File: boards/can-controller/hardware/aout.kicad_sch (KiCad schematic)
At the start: 23 parts, among them J50 ANALOG, U60 MCP4922-E/SL, U61 LM4040-2.5, U62 LM358B, U63 TPS61040

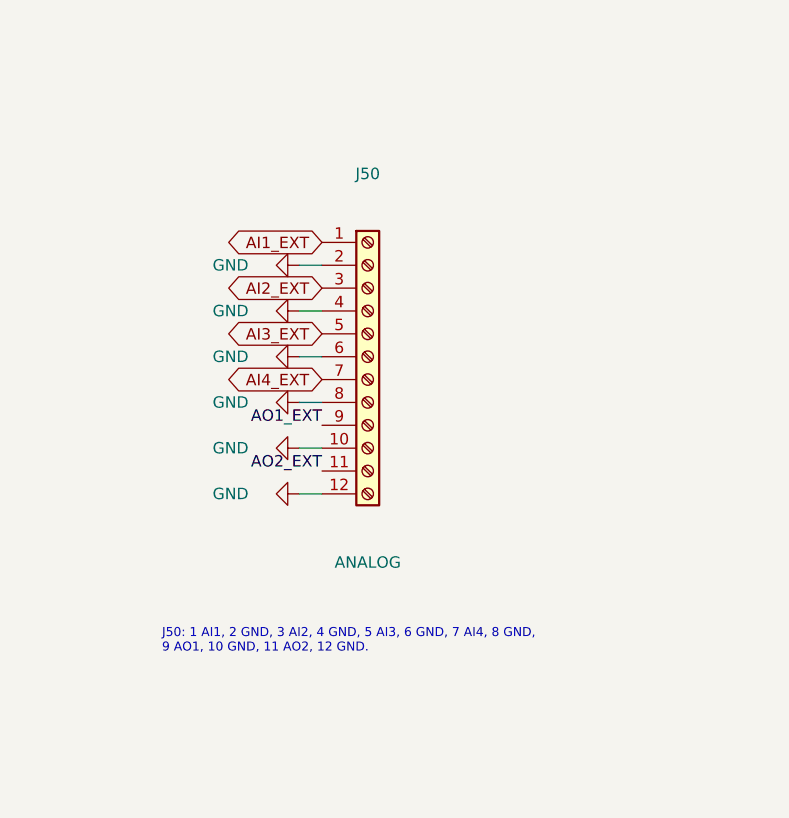
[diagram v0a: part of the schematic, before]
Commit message: can-controller: double-level push-in terminals, re-placement, no DIN clips
- Phoenix SPTD 1,5 footprints (3-8 positions) generated from the Phoenix
  drawing (lib/footprint_src/Thl_Connector/phoenix_sptd.py)
- Schematic: J40 GPIO 2x8 (GPIO1-8 / GND), J50 ANALOG 2x6 (AI1-4, AO1-2 /
  GND), J30 RELAY 2x8 (OUT1-8 / +12 V); relay LEDs moved to the 12 V side
  (+12 V -> 4.7k -> LED -> OUTn); J41 removed
- Placement rev 2: GPIO and analog on the left edge, relay on the bottom;
  12 V block x > 140, y > 160 plus the CAN strip; all ISO1044 on x = 168;
  relay LEDs behind their terminal pins; CAN LEDs in a column
- DIN clip holes removed (3D-printed adapter on the M2.5 holes instead)
- DRC clean apart from unrouted nets and silkscreen

Co-Authored-By: Claude Opus 5.5 <noreply@anthropic.com>
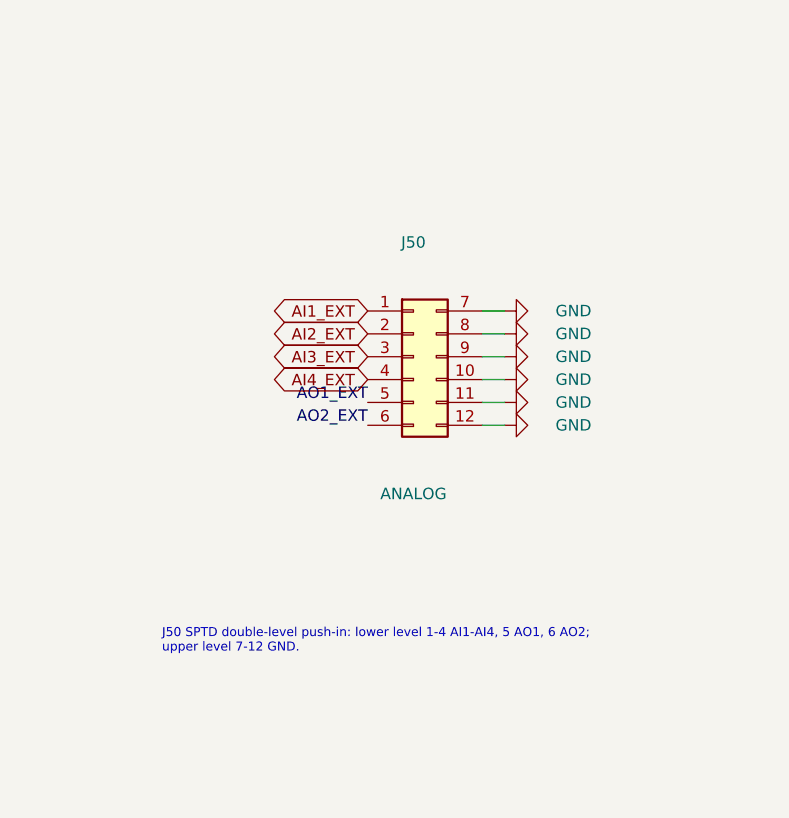
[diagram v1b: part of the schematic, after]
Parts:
- removed J50: ANALOG, Connector_Phoenix_MC:PhoenixContact_MC_1,5_12-G-3.5_1x12_P3.50mm_Horizontal, symbol Connector:Screw_Terminal_01x12
- added J50: ANALOG, Thl_Connector:PhoenixContact_SPTD_1,5_6-H-3,5_2x06_P3.5mm_Horizontal, symbol Connector_Generic:Conn_02x06_Top_Bottom
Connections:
- net AI1_EXT: now also J50.1 (Pin_1)
- net AI2_EXT: now also J50.2 (Pin_2)
- net AI3_EXT: now also J50.3 (Pin_3)
- net AI4_EXT: now also J50.4 (Pin_4)
- net AO1_EXT: now also J50.5 (Pin_5)
- net AO2_EXT: now also J50.6 (Pin_6)
- net GND: now also J50.10 (Pin_10), J50.11 (Pin_11), J50.12 (Pin_12), J50.7 (Pin_7), J50.8 (Pin_8), J50.9 (Pin_9)
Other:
- note added: "J50 SPTD double-level push-in: lower level 1-4 AI1-AI4, 5 AO1, 6 AO2; upper level 7-12 GND."
- note removed: "J50: 1 AI1, 2 GND, 3 AI2, 4 GND, 5 AI3, 6 GND, 7 AI4, 8 GND, 9 AO1, 10 GND, 11 AO2, 12 GND."

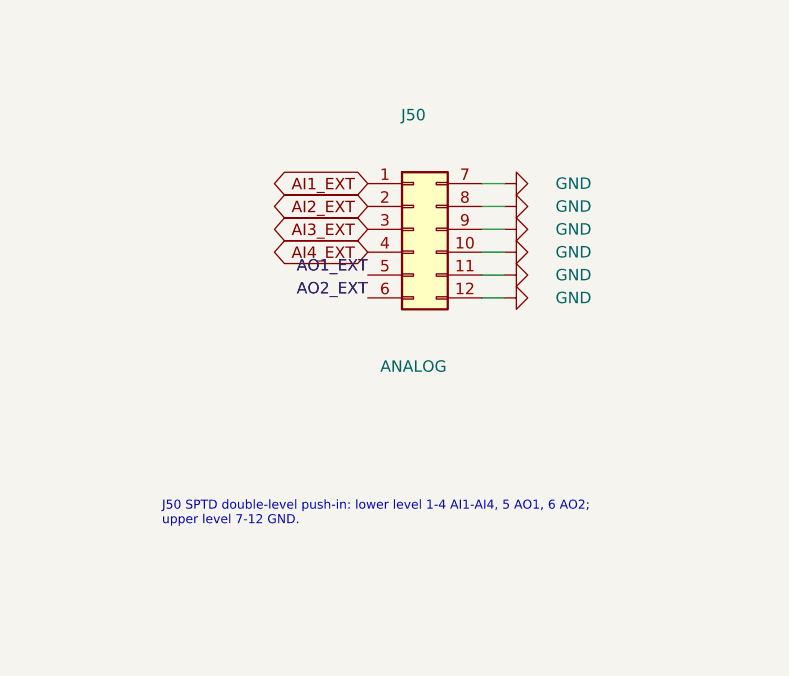
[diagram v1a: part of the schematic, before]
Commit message: can-controller: placement rev 3 so the MCU can fan out, routing WIP
Schematic:
- U1 pin map redone for the MCU rotated 90 deg: each side carries the
  signals for the parts it faces, in order (GPIO left, CAN right, USB /
  crystal / ICSP / UART top, DAC SPI4 / I2C1 bottom). ICSP on PGx2
  (pins 43/44, ICESEL = PGx2), UART1 on 46/47, V12_OK on pin 33.
- Relays driven over I2C1 by an MCP23008 (U33, 0x20); relay channel
  order permuted so expander -> ISO6740 -> ULN2803A -> J30 runs straight
- FB1 removed, AVDD tied to +3V3 (sits between two CAN pin pairs)
- J50 pinout: 1-2 AO1/AO2, 3-6 AI1-4 (outputs no longer cross inputs)
- Interface_Expansion:MCP23008-xSO imported to lib/

PCB:
- place_rev3.py: U1 rotated at (148,131), expander under it, relay
  isolators across the 12 V block's top edge (corner now x = 134),
  ULN below, 12 V opto at the top of the CAN strip, analog section
  re-laid around the new J50 pinout; bottom zones follow the new corner
- Routed: MCU escape nets first, signals top only, then power; 8
  connections open, ~48 clearance near-misses to clean up by hand,
  ~370 mm bottom traces

Co-Authored-By: Claude Opus 5.5 <noreply@anthropic.com>
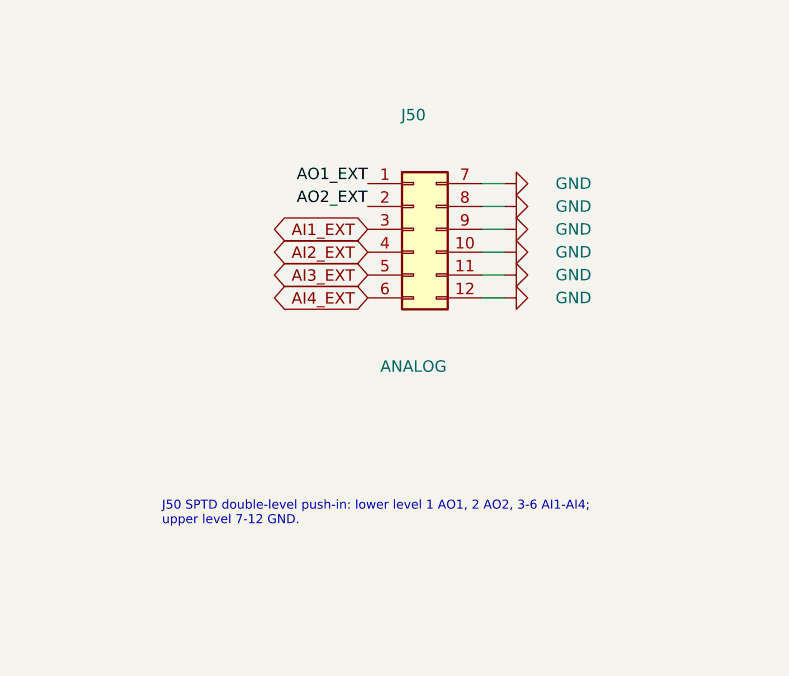
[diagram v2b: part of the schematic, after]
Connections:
- net AI1_EXT: now also J50.3 (Pin_3); no longer J50.1 (Pin_1)
- net AI2_EXT: now also J50.4 (Pin_4); no longer J50.2 (Pin_2)
- net AI3_EXT: now also J50.5 (Pin_5); no longer J50.3 (Pin_3)
- net AI4_EXT: now also J50.6 (Pin_6); no longer J50.4 (Pin_4)
- net AO1_EXT: now also J50.1 (Pin_1); no longer J50.5 (Pin_5)
- net AO2_EXT: now also J50.2 (Pin_2); no longer J50.6 (Pin_6)
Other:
- note added: "J50 SPTD double-level push-in: lower level 1 AO1, 2 AO2, 3-6 AI1-AI4; upper level 7-12 GND."
- note removed: "J50 SPTD double-level push-in: lower level 1-4 AI1-AI4, 5 AO1, 6 AO2; upper level 7-12 GND."
